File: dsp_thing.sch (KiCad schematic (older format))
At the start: 1 part

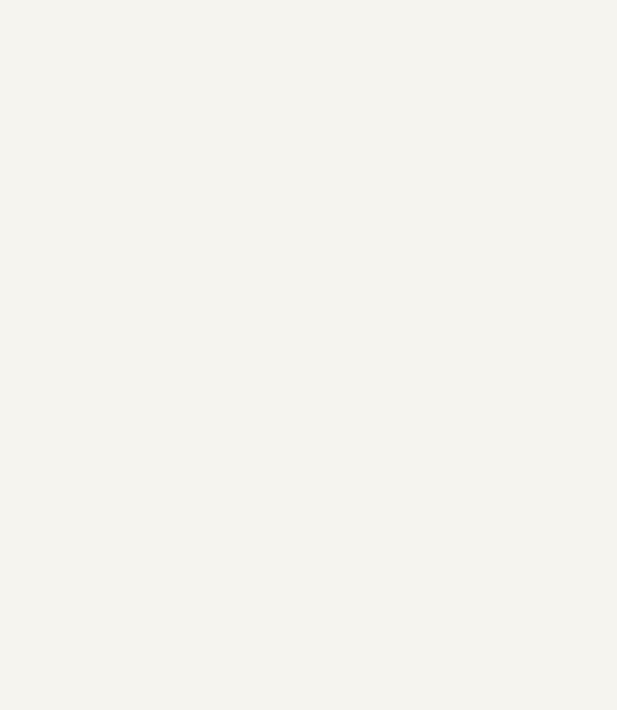
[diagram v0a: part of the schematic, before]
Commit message: Add audio_digital library and CP2615:
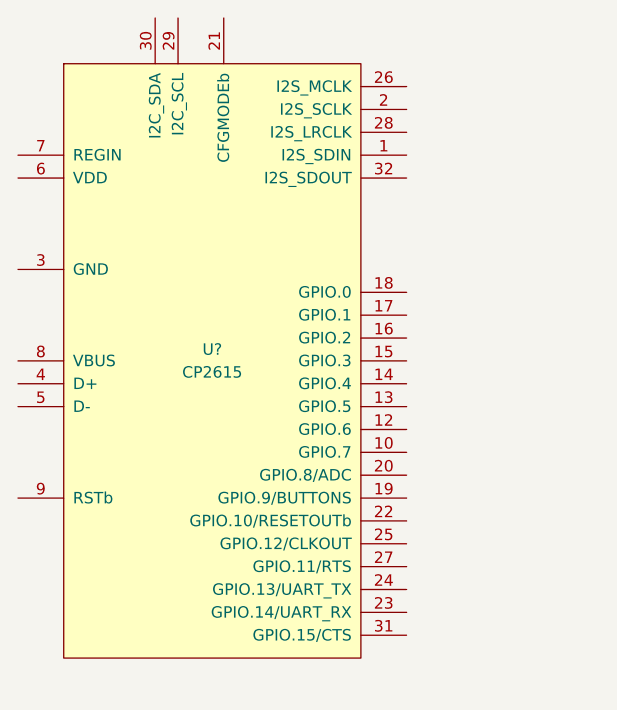
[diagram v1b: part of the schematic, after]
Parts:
- added U?: CP2615, Package_DFN_QFN:QFN-32-1EP_5x5mm_P0.5mm_EP3.7x3.7mm_ThermalVias, symbol audio_digital:CP2615
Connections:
- new net: U?.3 (GND), U?.GND (33)
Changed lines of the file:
@@
+	1    0    0    -1
+$EndComp
+$Comp
+L audio_digital:CP2615 U?
+U 1 1 5EC1F14B
+P 3950 5050
+F 0 "U?" H 3950 5100 50  0000 C CNN
+F 1 "CP2615" H 3950 5000 50  0000 C CNN
+F 2 "Package_DFN_QFN:QFN-32-1EP_5x5mm_P0.5mm_EP3.7x3.7mm_ThermalVias" H 7150 4900 50  0001 C CNN
+F 3 "https://www.silabs.com/documents/public/data-sheets/cp2615-datasheet.pdf" H 7150 4900 50  0001 C CNN
+	1    3950 5050
 	1    0    0    -1
 $EndComp

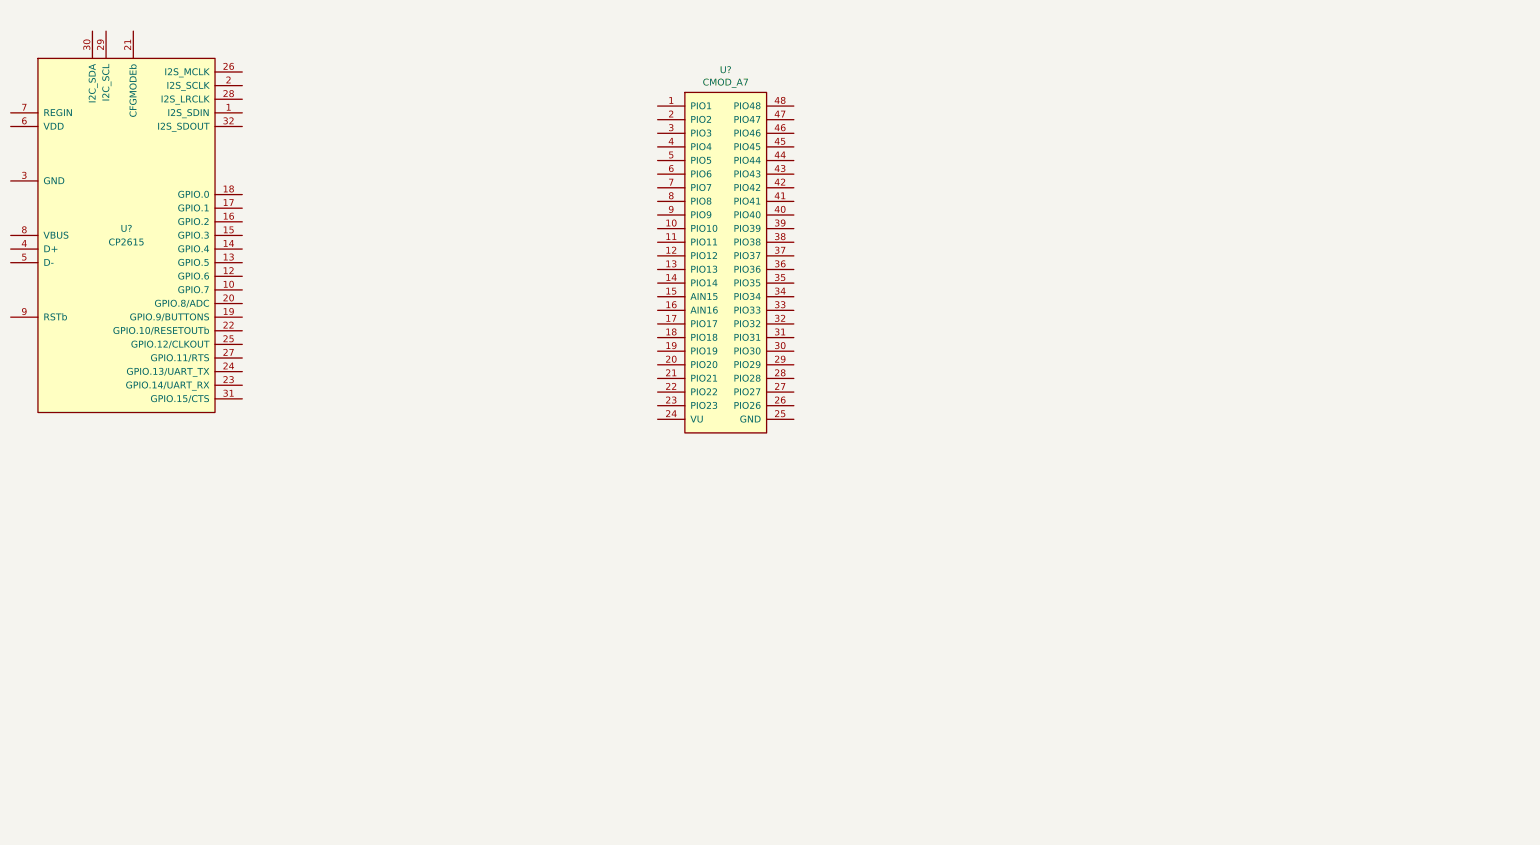
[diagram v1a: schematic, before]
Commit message: Add CS4350 DAC to schematic
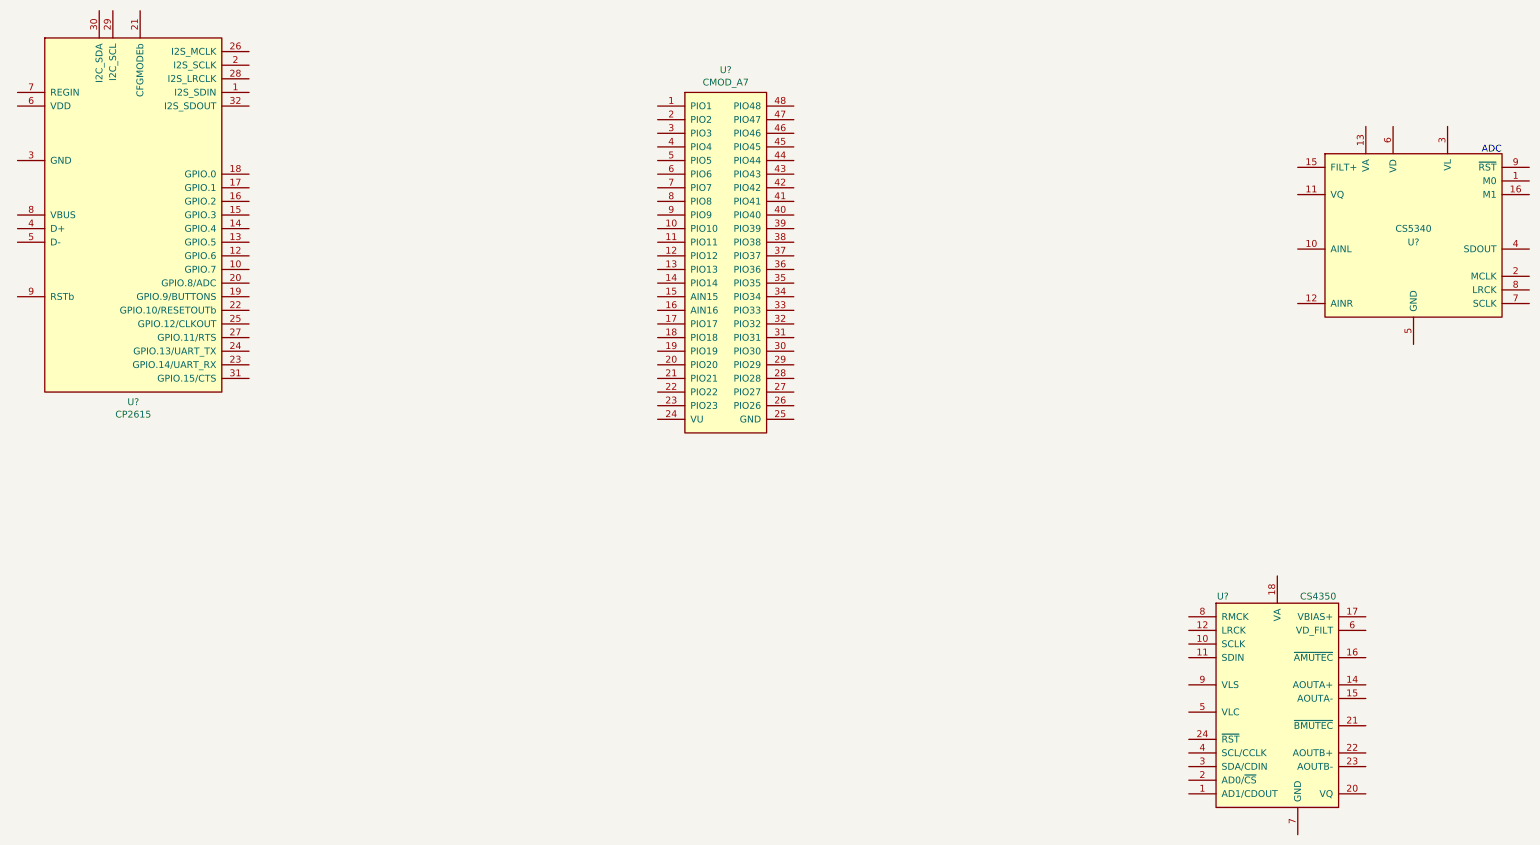
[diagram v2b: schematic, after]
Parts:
- removed U?: CP2615, Package_DFN_QFN:QFN-32-1EP_5x5mm_P0.5mm_EP3.7x3.7mm_ThermalVias, symbol audio_digital:CP2615
- added U?: CS5340, Package_SO:TSSOP-16_4.4x5mm_P0.65mm, symbol audio_digital:CS5340
- added U?: CP2615, Package_DFN_QFN:QFN-32-1EP_5x5mm_P0.5mm_EP3.7x3.7mm_ThermalVias, symbol audio_digital:CP2615
- added U?: CS4350, Package_SO:TSSOP-24_4.4x7.8mm_P0.65mm, symbol audio_digital:CS4350
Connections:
- new net: U?.14 (GND), U?.5 (GND)
- new net: U?.3 (GND), U?.GND (33)
- new net: U?.19 (GND), U?.7 (GND)
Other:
- note added: "ADC"
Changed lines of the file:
@@
+$EndComp
+$Comp
+L audio_digital:CS5340 U?
+U 1 1 5EC242DE
+P 13400 5050
+F 0 "U?" H 13400 5000 50  0000 C CNN
+F 1 "CS5340" H 13400 5100 50  0000 C CNN
+F 2 "Package_SO:TSSOP-16_4.4x5mm_P0.65mm" H 13900 5450 50  0001 C CNN
+F 3 "https://statics.cirrus.com/pubs/proDatasheet/CS5340_F2.pdf" H 13900 5450 50  0001 C CNN
+	1    13400 5050
+	1    0    0    -1
 $EndComp
 $Comp
 L audio_digital:CP2615 U?
-U 1 1 5EC1F14B
-P 3950 5050
-F 0 "U?" H 3950 5100 50  0000 C CNN
-F 1 "CP2615" H 3950 5000 50  0000 C CNN
-F 2 "Package_DFN_QFN:QFN-32-1EP_5x5mm_P0.5mm_EP3.7x3.7mm_ThermalVias" H 7150 4900 50  0001 C CNN
-F 3 "https://www.silabs.com/documents/public/data-sheets/cp2615-datasheet.pdf" H 7150 4900 50  0001 C CNN
-	1    3950 5050
+U 1 1 5EC2493D
+P 4000 4900
+F 0 "U?" H 4000 3527 50  0000 C CNN
+F 1 "CP2615" H 4000 3436 50  0000 C CNN
+F 2 "Package_DFN_QFN:QFN-32-1EP_5x5mm_P0.5mm_EP3.7x3.7mm_ThermalVias" H 7200 4750 50  0001 C CNN
+F 3 "https://www.silabs.com/documents/public/data-sheets/cp2615-datasheet.pdf" H 7200 4750 50  0001 C CNN
+	1    4000 4900
 	1    0    0    -1
 $EndComp
+Text Notes 13900 4450 0    50   ~ 0
+ADC
+$Comp
+L audio_digital:CS4350 U?
+U 1 1 5EC29963
+P 12400 8500
+F 0 "U?" H 12000 9300 50  0000 C CNN
+F 1 "CS4350" H 12700 9300 50  0000 C CNN
+F 2 "Package_SO:TSSOP-24_4.4x7.8mm_P0.65mm" H 12400 9400 50  0001 C CNN
+F 3 "https://statics.cirrus.com/pubs/proDatasheet/CS4350_F4.pdf" H 13900 10900 50  0001 C CNN
+	1    12400 8500
+	1    0    0    -1
+$EndComp
